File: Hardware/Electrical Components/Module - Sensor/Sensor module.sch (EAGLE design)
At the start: 29 parts

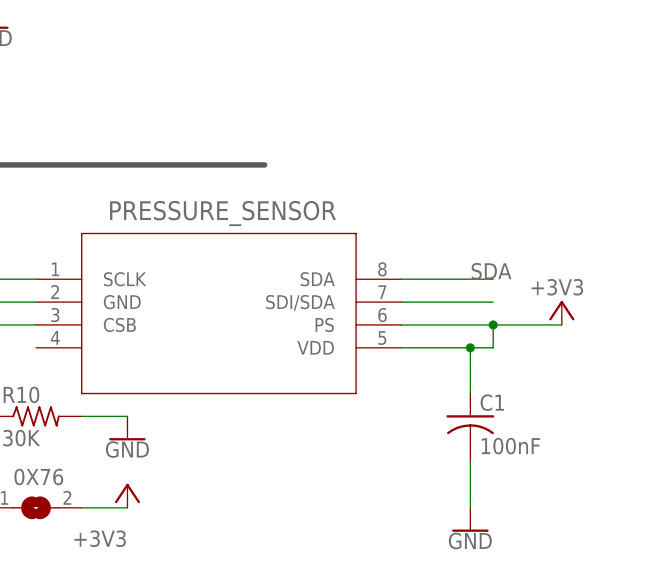
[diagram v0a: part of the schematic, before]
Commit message: Major fix for sensor module
O Power Module: Changes in footprint location of motor push-to-connect for mounting place. Move the 90-angle header further inside for better mechanical support
O Sensor Module: Rearrange 2.5mm headphone jack closer to the edge for proper mounting. The older version stops the male jack fully dock with the female casing thus fail to connect. Move the 90-angle header further inside for better mechanical support.
O MS5803-02BA: Change symbol, change SDA -> SDO. This label caused the PCB to stop working with all I2C devices. Sensor Module: Rewire to the write SDA, tested.
+ Add MS5803-02BA Datasheet
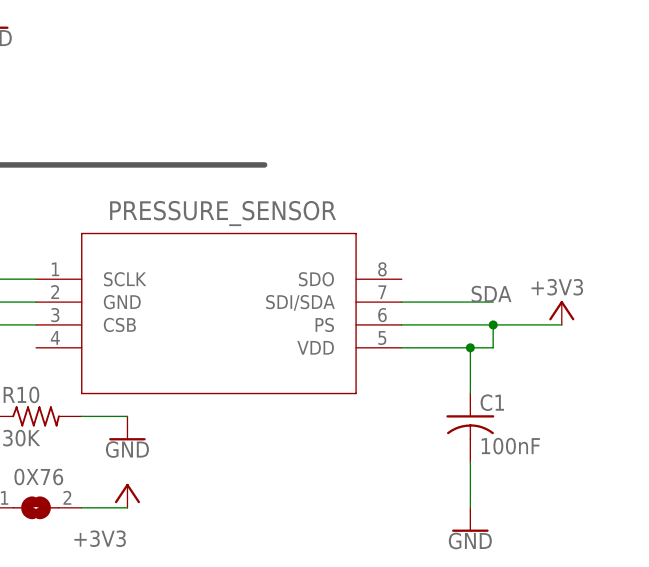
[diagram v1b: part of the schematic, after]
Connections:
- removed net N$11: PRESSURE_SENSOR.SDI/SDA
- net SDA: now also PRESSURE_SENSOR.SDI/SDA; no longer PRESSURE_SENSOR.SDA
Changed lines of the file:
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@@
 </segment>
 <segment>
-<pinref part="PRESSURE_SENSOR" gate="A" pin="SDA"/>
-<wire x1="165.1" y1="-40.64" x2="175.26" y2="-40.64" width="0.1524" layer="91"/>
-<label x="172.72" y="-40.64" size="1.778" layer="95"/>
+<pinref part="PRESSURE_SENSOR" gate="A" pin="SDI/SDA"/>
+<wire x1="165.1" y1="-43.18" x2="175.26" y2="-43.18" width="0.1524" layer="91"/>
+<label x="172.72" y="-43.18" size="1.778" layer="95"/>
 </segment>
 </net>
@@
 </segment>
 </net>
-<net name="N$11" class="0">
-<segment>
-<pinref part="PRESSURE_SENSOR" gate="A" pin="SDI/SDA"/>
-<wire x1="165.1" y1="-43.18" x2="175.26" y2="-43.18" width="0.1524" layer="91"/>
-</segment>
-</net>
